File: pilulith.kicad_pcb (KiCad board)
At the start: 6 copper layers, 22.1 x 22.1 mm, 91 parts, among them J101 Conn_01x03_Pin, J103 Conn_ARM_JTAG_SWD_10, Q1 SBC847, SW1 KMT221NG, SW2 KMT221NG, U1 NRF54L15-QFAA-R, U10 LIS2DH, U102 WLA.04, U103 ATECC608B-MAHDA, U104 LF21115TMR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

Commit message: initial routing complete
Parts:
- removed C103: 10U, Capacitor_SMD:C_0805_2012Metric
- removed C106, C110, C112: 0.1U, Capacitor_SMD:C_0201_0603Metric
- removed C111: 4U7, Capacitor_SMD:C_0603_1608Metric
- removed C113, C114, C115, C116: 12P, Capacitor_SMD:C_0201_0603Metric
- removed TP1, TP16, TP17, TP18, TP19, TP2, TP20, TP3, TP4, TP5, TP6, TP7, TP8, TP9: TestPoint, TestPoint:TestPoint_Pad_D1.5mm
- added C3: 2U2, Capacitor_SMD:C_0201_0603Metric, F.Cu at (158.4, 93.7)
- added C4: 10N, Capacitor_SMD:C_0201_0603Metric, F.Cu at (159.9, 94.4)
- added C5: 2N2, Capacitor_SMD:C_0201_0603Metric, F.Cu at (165.6, 97.0)
- added C6: 0.1U, Capacitor_SMD:C_0201_0603Metric, F.Cu at (155.1, 99.9)
- added C7: 2U2, Capacitor_SMD:C_0201_0603Metric, F.Cu at (155.0, 94.5)
- added C8: 1P2, Capacitor_SMD:C_0201_0603Metric, F.Cu at (167.1, 99.2)
- added C9: 0.1U, Capacitor_SMD:C_0201_0603Metric, F.Cu at (160.8, 102.4)
- added L1: FB, Inductor_SMD:L_0201_0603Metric, F.Cu at (158.5, 94.4)
- added L3: 4U7, Inductor_SMD:L_0402_1005Metric, F.Cu at (156.8, 94.3)
- added L4: 2N0, Inductor_SMD:L_0201_0603Metric, F.Cu at (168.1, 99.6)
- added LED13: RED, LED_SMD:LED_0201_0603Metric, F.Cu at (159.3, 102.4)
- added LED14: RED, LED_SMD:LED_0201_0603Metric, F.Cu at (161.2, 104.0)
- added LED15: RED, LED_SMD:LED_0201_0603Metric, F.Cu at (159.5, 105.7)
- added LED16: RED, LED_SMD:LED_0201_0603Metric, F.Cu at (157.8, 104.0)
- added R1: R_Small, Resistor_SMD:R_0201_0603Metric, F.Cu at (157.9, 102.4)
- added R2: R_Small, Resistor_SMD:R_0201_0603Metric, F.Cu at (157.4, 105.9)
- added R3: R_Small, Resistor_SMD:R_0201_0603Metric, F.Cu at (157.0, 104.0)
- added R5: R_Small, Resistor_SMD:R_0201_0603Metric, F.Cu at (162.0, 104.0)
- added SW3: KMT221NG, Button_Switch_SMD:SW_Push_1P1T_NO_CK_KMR2, B.Cu at (151.9, 99.3)
- added SW4: KMT221NG, pilulith:SW_EVP-AWED4A, F.Cu at (164.0, 106.0)
- C108: value 1U -> 10U
- C117: value 12P -> 1P2
- G***: moved to F.Cu
- moved TP15 18.5 mm to (160.4, 113.6)
- moved U105 17.3 mm to (165.9, 110.7), turned to -45 degrees
- moved TP14 17.0 mm to (156.7, 113.4)
- moved U104 17.0 mm to (167.9, 106.3), turned to -22.5 degrees
- moved SW1 16.7 mm to (165.4, 97.5), turned to 135 degrees
- moved SW2 16.6 mm to (165.7, 110.4), turned to 45 degrees
- moved U106 16.3 mm to (151.2, 101.7), turned to -105 degrees
- moved C102 16.0 mm to (151.1, 106.3), turned to -165 degrees
- moved C108 11.4 mm to (154.2, 96.4), turned to 180 degrees
- moved C107 11.2 mm to (155.5, 95.6), turned to 90 degrees
- moved R114 10.3 mm to (152.8, 97.7), turned to 90 degrees
- moved C118 9.79 mm to (164.1, 109.9), turned to 45 degrees
- moved G*** 9.43 mm to (165.1, 102.1), turned to 120 degrees
- moved C101 8.99 mm to (163.4, 95.3), turned to 90 degrees
- moved R113 8.95 mm to (153.5, 97.7), turned to -90 degrees
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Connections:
- C107 pad 1: unconnected-(C107-Pad1) -> VCC
- C108 pad 1: /DEC4_6 -> VCC
- L102 pad 2: /ANT_FEED -> Net-(C8-Pad2)
- R113 pad 1: Net-(U1-P1.11/ASO(3)/RADIO(2)/AIN4) -> /BATTERY_MEAS
- R114 pad 2: Net-(U1-P1.11/ASO(3)/RADIO(2)/AIN4) -> /BATTERY_MEAS
- U1 pad 10: Net-(U1-VDD-Pad10) -> VCC
- U1 pad 11: /LED03 -> /LED11
- U1 pad 12: /LED08 -> /LED10
- U1 pad 13: /LED07 -> /LED09
- U1 pad 14: /LED06 -> /LED08
- U1 pad 15: /LED10 -> /LED07
- U1 pad 16: /LED11 -> /LED06
- U1 pad 17: /2.06/TC -> /LED05
- U1 pad 22: Net-(U1-VDD-Pad10) -> VCC
- U1 pad 28: /LED05 -> /LED03
- U1 pad 32: unconnected-(U1-VSS_PA-Pad32) -> GND
- U1 pad 33: unconnected-(U1-DECRF-Pad33) -> DECA
- U1 pad 36: Net-(U1-VDD-Pad10) -> VCC
- U1 pad 37: /LED01 -> /LED02
- U1 pad 38: /LED02 -> /LED01
- U1 pad 39: Net-(U1-P1.11/ASO(3)/RADIO(2)/AIN4) -> /IMU_INT
- U1 pad 43: unconnected-(U1-DECA-Pad43) -> DECA
- U1 pad 44: Net-(U1-VSS-Pad44) -> GND
- U1 pad 45: unconnected-(U1-DECD-Pad45) -> DECD
- U1 pad 46: unconnected-(U1-DCC-Pad46) -> DCC
- U1 pad 47: Net-(U1-VDD-Pad10) -> VCC
- U1 pad 48: Net-(U1-VDD-Pad10) -> VCC
- U1 pad 49: Net-(U1-VSS-Pad44) -> GND
- U1 pad 7: /IMU_INT -> /BATTERY_MEAS
- Y101 pad 2: GND -> unconnected-(Y101-Pad2)
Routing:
- net /BOOT: track 0.00 -> 52.6 mm, vias 0 -> 7
- net /SCL: track 0.00 -> 27.9 mm, vias 0 -> 5
- net /SDA: track 0.00 -> 23.6 mm, vias 0 -> 4
- net /MAG: track 0.00 -> 19.4 mm, vias 0 -> 3
- net /IMU_INT: track 0.00 -> 18.8 mm, vias 0 -> 3
- net VCC: track 0.00 -> 18.8 mm, vias 0 -> 21
- net /nRF52_RX: track 0.00 -> 18.4 mm, vias 0 -> 4
- net GND: track 0.00 -> 17.4 mm, vias 0 -> 52
- net /LED04: track 0.00 -> 17.3 mm, vias 0 -> 4
- net /LED05: track 0.00 -> 16.9 mm, vias 0 -> 3
- net /nRF52_TX: track 0.00 -> 16.6 mm, vias 0 -> 2
- net /SWCLK: track 0.00 -> 15.3 mm, vias 0 -> 2
- net /NFC1: track 0.00 -> 14.6 mm, vias 0 -> 3
- net /LED08: track 0.00 -> 14.3 mm, vias 0 -> 3
- net /LED06: track 0.00 -> 14.2 mm, vias 0 -> 2
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- removed copper zone on F.Cu, net VCC
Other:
- board text added: "HSM"
- board text added: "nRF54L"
- board text removed: "0.07"
- board text removed: "1.00"
- board text removed: "Boot/User"
- board text removed: "GND"
- board text removed: "SWCLK"
- board text removed: "SWDIO"
- board text removed: "VCC"

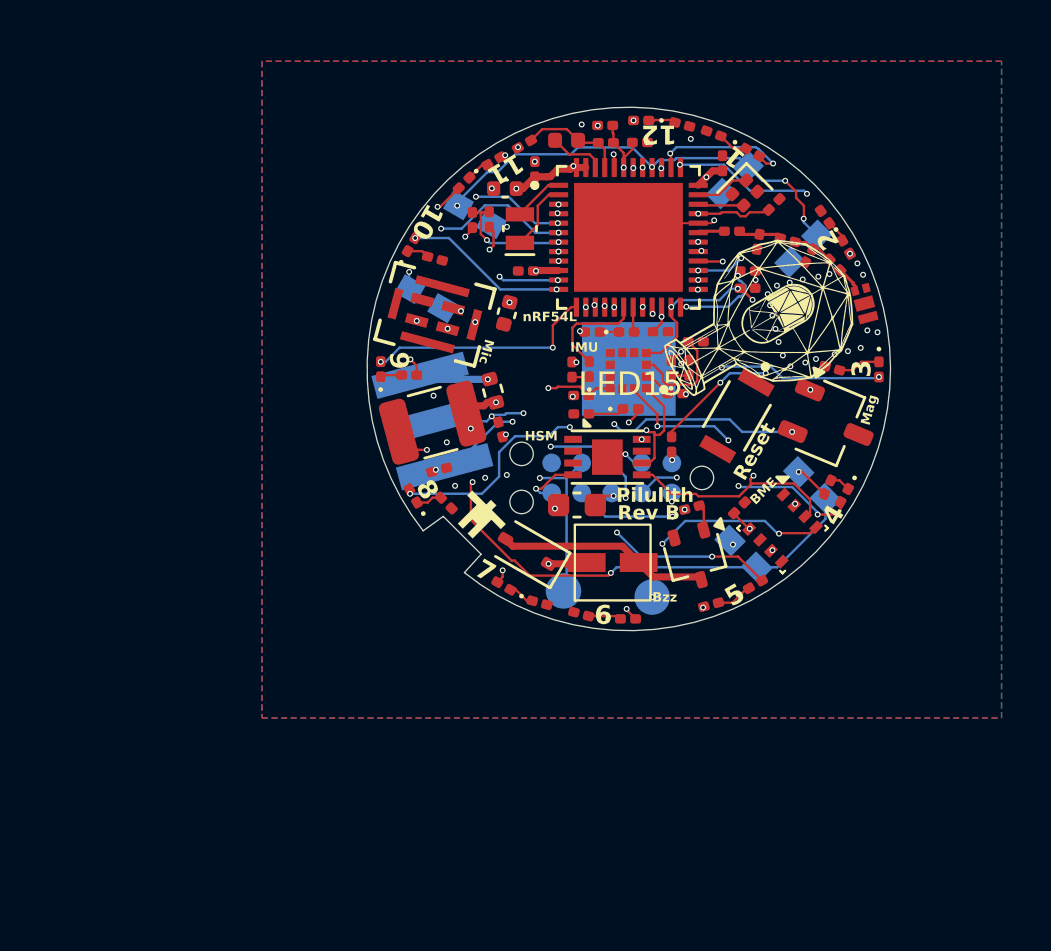
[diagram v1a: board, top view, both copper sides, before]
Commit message: putting in a no popped npm2100 for future proofing
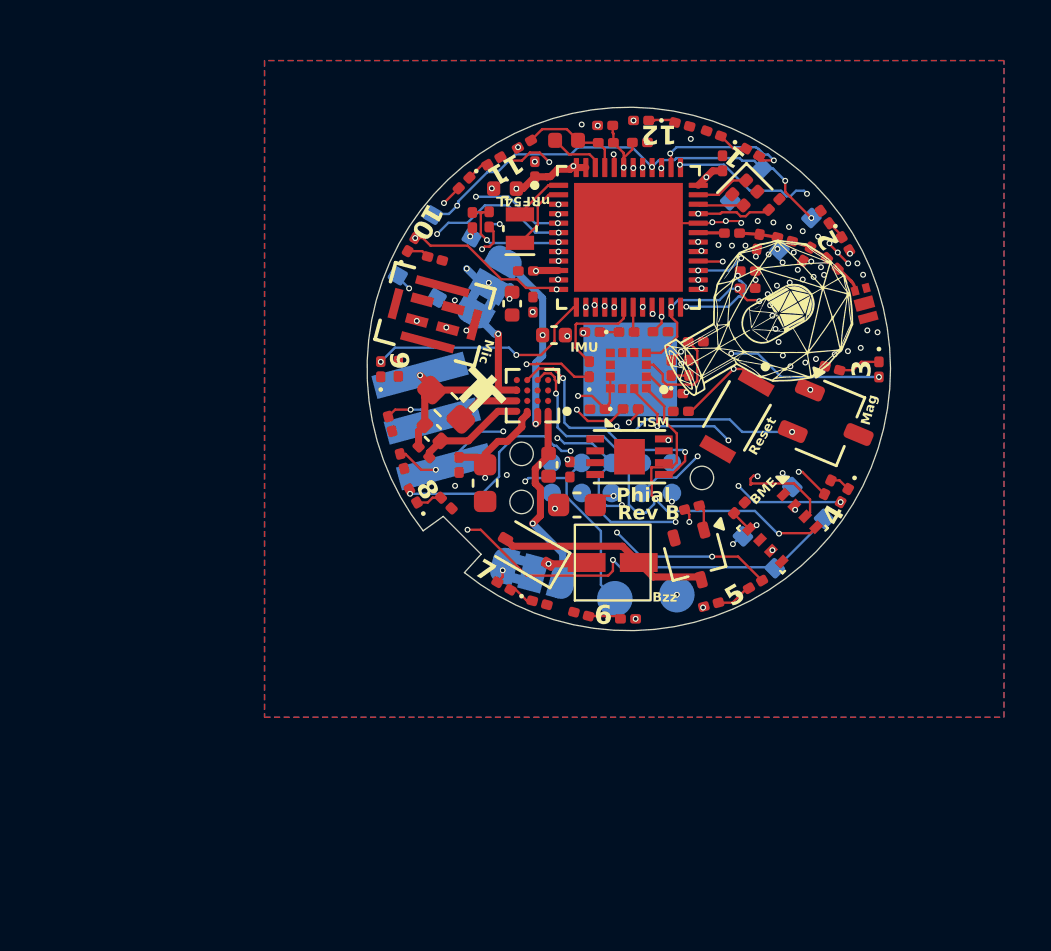
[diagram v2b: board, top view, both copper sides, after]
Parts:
- removed C102: 100U, Capacitor_SMD:C_1210_3225Metric
- removed R116: 0, Resistor_SMD:R_0402_1005Metric
- added C10: 22U, Capacitor_SMD:C_0603_1608Metric, F.Cu at (153.4, 108.8)
- added C11: 1N, Capacitor_SMD:C_0201_0603Metric, F.Cu at (150.8, 107.5)
- added C12: 10U, Capacitor_SMD:C_0402_1005Metric, F.Cu at (151.2, 106.7)
- added C13: 2U2, Capacitor_SMD:C_0402_1005Metric, F.Cu at (156.0, 108.0)
- added C14: 2U2, Capacitor_SMD:C_0402_1005Metric, F.Cu at (156.3, 102.6)
- added C16: 1N, Capacitor_SMD:C_0201_0603Metric, F.Cu at (152.3, 108.1)
- added G***: LOGO, orleon:the_golioth_2mm, B.Cu at (168.2, 109.0)
- added G***: LOGO, orleon:the_golioth_2mm, B.Cu at (151.1, 109.8)
- added JP1: npm2100-bridge, Jumper:SolderJumper-3_P1.3mm_Bridged2Bar12_RoundedPad1.0x1.5mm, B.Cu at (153.5, 100.5)
- added JP2: sensor-bridge, Jumper:SolderJumper-3_P1.3mm_Bridged2Bar12_RoundedPad1.0x1.5mm, B.Cu at (155.4, 112.6)
- added L2: 2u2, Inductor_SMD:L_0603_1608Metric_Pad1.05x0.95mm_HandSolder, F.Cu at (151.7, 105.5)
- added U2: NPM2100-CAAA-R, pilulith:BGA16N44P4X4_189X191X52N, F.Cu at (155.4, 105.1)
- SW1, SW2, SW3: footprint Button_Switch_SMD:SW_Push_1P1T_NO_CK_KMR2 -> pilulith:KMT221NG
- moved G*** 10.8 mm to (159.5, 93.8), turned to 0 degrees
- moved G*** 5.30 mm to (153.2, 104.9)
- moved C2 4.66 mm to (149.4, 106.3)
- moved R3 3.20 mm to (155.4, 101.3)
- moved R2 2.39 mm to (156.9, 108.2), turned to -90 degrees
- moved TP14 2.19 mm to (158.8, 113.7)
- moved C1 1.61 mm to (149.9, 107.9), turned to -75 degrees
- moved R66 1.45 mm to (161.6, 105.8), turned to 180 degrees
- moved TP15 1.04 mm to (161.5, 113.5)
- moved U103 0.94 mm to (159.5, 107.7)
- moved C105 0.90 mm to (158.1, 105.7)
- moved SW3 0.67 mm to (151.2, 99.2)
- moved R109 0.53 mm to (149.7, 104.0), turned to 90 degrees
- moved C104 0.47 mm to (154.5, 101.2), turned to -90 degrees
- moved SW2 0.42 mm to (166.0, 110.7)
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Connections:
- C104 pad 1: VCC -> VSENSOR
- C105 pad 1: VCC -> VSENSOR
- C118 pad 1: VCC -> VSENSOR
- C29 pad 1: VCC -> VSENSOR
- D3 pad 1: VCC -> VSENSOR
- LS1 pad 1: VCC -> VSENSOR
- R115 pad 2: VCC -> VSENSOR
- R117 pad 1: VCC -> VSENSOR
- R118 pad 1: VCC -> VSENSOR
- U10 pad 10: VCC -> VSENSOR
- U10 pad 9: VCC -> VSENSOR
- U103 pad 8: VCC -> VSENSOR
- U104 pad 1: VCC -> VSENSOR
- U105 pad 6: VCC -> VSENSOR
- U105 pad 8: VCC -> VSENSOR
- U106 pad 1: VCC -> VSENSOR
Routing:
- net /VOUT-NPM2100: track 0.00 -> 8.26 mm, vias 0 -> 2
- net /VOUTLDO-NPM2100: track 0.00 -> 8.18 mm, vias 0 -> 1
- net VSENSOR: track 0.00 -> 8.05 mm, vias 0 -> 11
- net /CR2032_V+: track 3.06 -> 10.9 mm, vias 1 -> 2
- net VCC: track 18.8 -> 11.7 mm, vias 21 -> 10
- net /SDA: track 23.6 -> 30.0 mm, vias 4 -> 6
- net /NFC1: track 14.6 -> 20.1 mm
- net /SCL: track 27.9 -> 33.0 mm
- net Net-(U2-PVSS): track 0.00 -> 4.62 mm
- net Net-(LED16-K): track 0.74 -> 5.24 mm, vias 0 -> 2
- net /VINT-NPM2100: track 0.00 -> 4.46 mm
- net Net-(LED15-K): track 1.53 -> 4.90 mm, vias 0 -> 2
- net GND: track 17.4 -> 14.3 mm, vias 52 -> 66
- net /nRF52_TX: track 16.6 -> 19.6 mm
- net /SW: track 0.00 -> 2.69 mm
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- added copper zone on In2.Cu, net VSENSOR
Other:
- board text added: "Phial"
- board text removed: "Pilulith"
- board text removed: "RST"

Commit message: rev b first pass done with no violatio ns
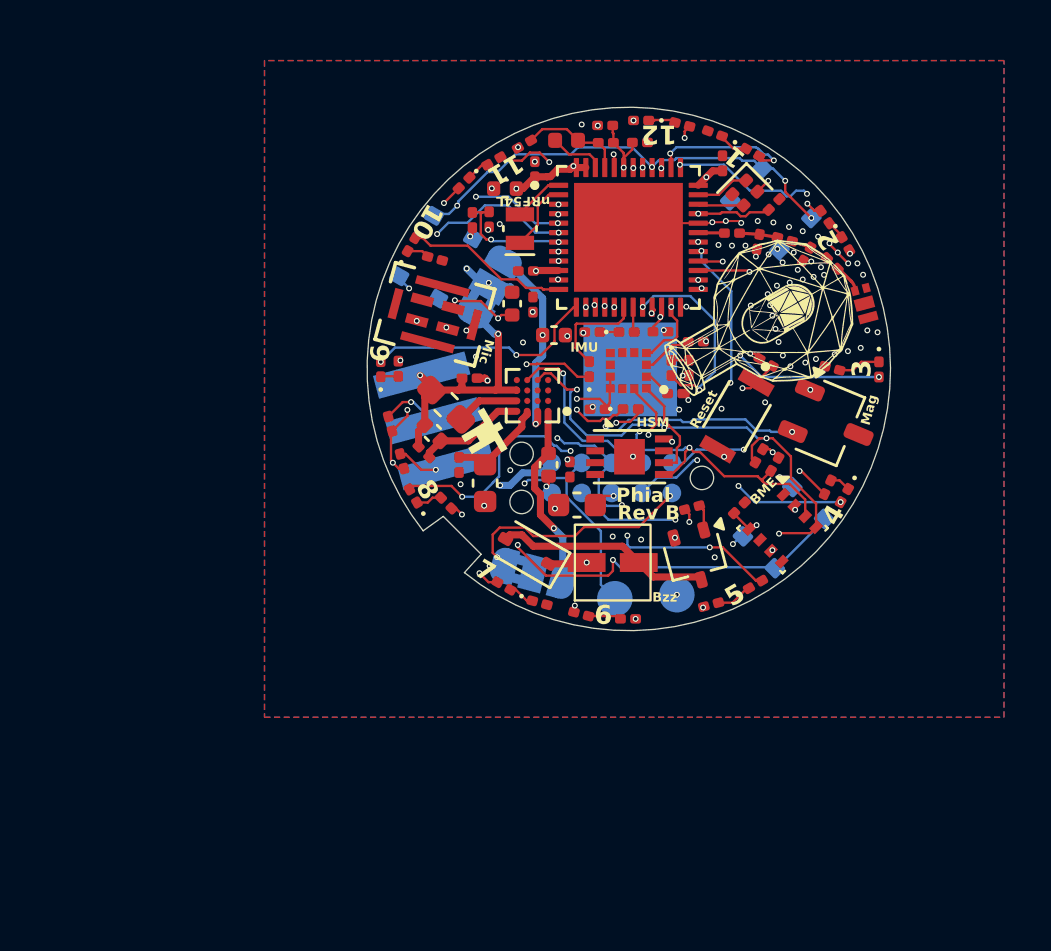
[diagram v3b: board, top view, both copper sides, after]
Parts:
- added R6: 0, Resistor_SMD:R_0201_0603Metric, F.Cu at (152.7, 104.4)
- moved R117 7.82 mm to (164.9, 107.7), turned to -120 degrees
- moved R118 7.53 mm to (165.6, 108.0), turned to -120 degrees
- moved R66 4.15 mm to (165.2, 103.7), turned to 150 degrees
- moved G*** 1.85 mm to (153.3, 106.8), turned to -60 degrees
- moved J101 0.07 mm to (151.2, 106.2)
- moved SW3 0.07 mm to (151.3, 99.3)
- turned C104 to 90 degrees
- turned LED14 to -90 degrees
- turned R5 to -90 degrees
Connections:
- J103 pad 6: unconnected-(J103-SWO/TDO-Pad6) -> /Power_Insert
- U105 pad 2: VCC -> VSENSOR
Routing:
- net GND: track 14.3 -> 24.7 mm, vias 66 -> 89
- net VCC: track 11.7 -> 20.7 mm, vias 10 -> 11
- net Net-(J103-~{RESET}): track 0.00 -> 7.92 mm, vias 0 -> 2
- net /Power_Insert: track 0.00 -> 7.70 mm, vias 0 -> 2
- net /2.09/T2: track 3.84 -> 8.35 mm
- net VSENSOR: track 8.05 -> 11.2 mm, vias 11 -> 12
- net /NFC1: track 20.1 -> 17.0 mm, vias 3 -> 2
- net Net-(U10-SDO/SA0): track 4.55 -> 2.17 mm
- net /SCL: track 33.0 -> 31.0 mm
- net /IMU_INT: track 17.8 -> 16.1 mm, vias 3 -> 2
- net /SDA: track 30.0 -> 28.7 mm, vias 6 -> 4
- net /LED07: track 13.6 -> 15.0 mm
- net /RESET_N: track 9.94 -> 8.74 mm
- net /2.10/T3: track 6.03 -> 6.97 mm
- net Net-(D109-K): track 0.10 -> 0.85 mm
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
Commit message: added second notch and moved associated components
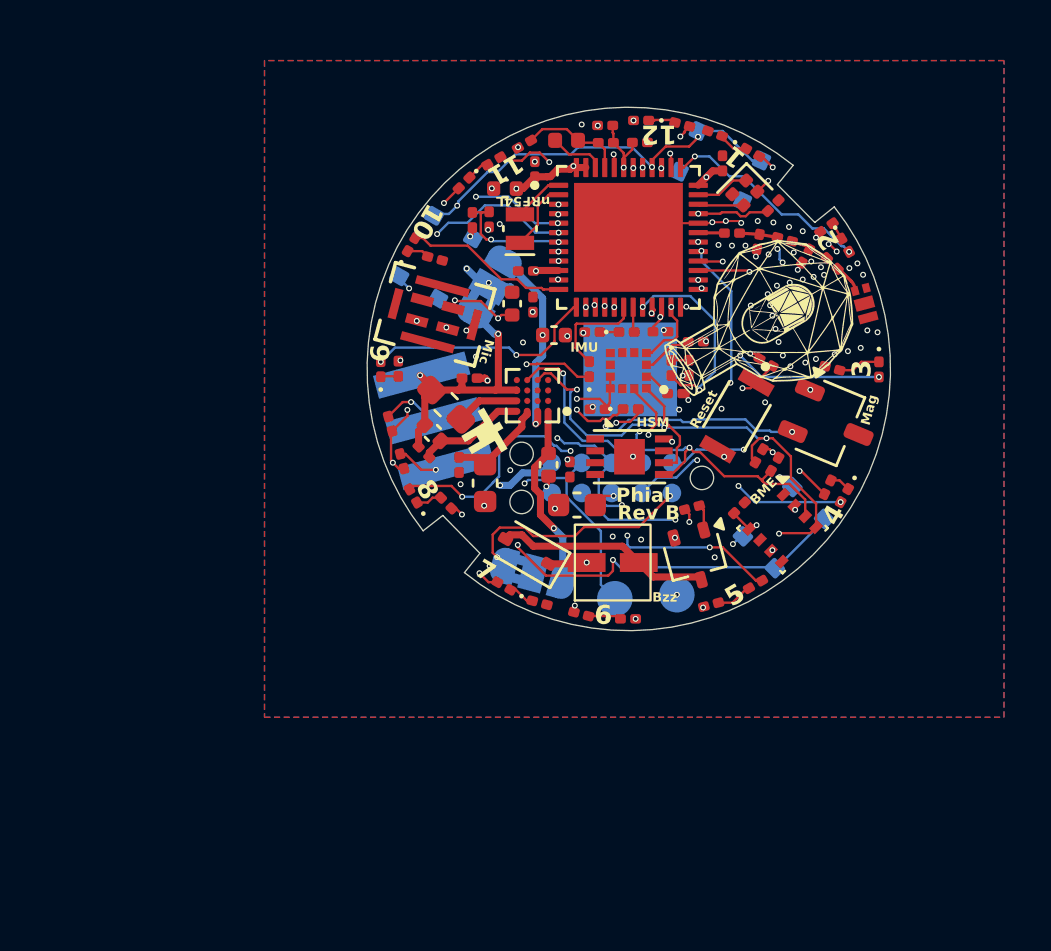
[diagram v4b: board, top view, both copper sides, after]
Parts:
- moved SW1 2.80 mm to (163.3, 95.4), turned to 155 degrees
- moved R102 0.45 mm to (167.8, 98.0), turned to -145 degrees
- moved C8 0.09 mm to (166.9, 99.2)
- moved C5 0.06 mm to (165.5, 97.1)
- moved D102 0.06 mm to (168.6, 98.8)
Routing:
- net /BOOT: track 53.9 -> 51.8 mm, vias 7 -> 6
- net GND: track 24.7 -> 23.4 mm, vias 89 -> 88
- net /LED02: track 9.50 -> 9.06 mm, vias 3 -> 2
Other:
- outline, holes or cut-outs redrawn

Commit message: add updated spirulo design into 3d space
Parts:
- moved G*** 1.47 mm to (167.6, 107.7)
- moved G*** 1.27 mm to (152.4, 109.7), turned to 135 degrees
- moved G*** 0.94 mm to (159.5, 94.8)
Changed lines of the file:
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@@
+			)
+		)
+		(model "${KIPRJMOD}/input/3d/spirulo-b-202601201651.step"
+			(offset
+				(xyz 0 0 4)
+			)
+			(scale
+				(xyz 1 1 1)
+			)
+			(rotate
+				(xyz -0 -0 -80)
 			)
 		)
@@
 	(footprint "orleon:the_golioth_2mm"
 		(layer "B.Cu")
-		(at 159.514483 93.807892)
+		(at 159.545315 94.75)
 		(property "Reference" "G***"
 			(at 0 0 0)
@@
 	(footprint "orleon:the_golioth_2mm"
 		(layer "B.Cu")
-		(at 168.22407 109.042462 -120)
+		(at 167.595315 107.71 -120)
 		(property "Reference" "G***"
 			(at 0 0 60)
@@
 	(footprint "orleon:the_golioth_2mm"
 		(layer "B.Cu")
-		(at 151.145315 109.8 120)
+		(at 152.405315 109.67 135)
 		(property "Reference" "G***"
-			(at 0 0 120)
+			(at 0 0 135)
 			(layer "B.SilkS")
 			(hide yes)
@@
 		)
 		(property "Value" "LOGO"
-			(at 0.75 0 120)
+			(at 0.75 0 135)
 			(layer "B.SilkS")
 			(hide yes)
@@
 		)
 		(property "Datasheet" ""
-			(at 0 0 120)
+			(at 0 0 135)
 			(layer "B.Fab")
 			(hide yes)
@@
 		)
 		(property "Description" ""
-			(at 0 0 120)
+			(at 0 0 135)
 			(layer "B.Fab")
 			(hide yes)
@@
 		(fp_poly
 			(pts
-				(xy 0.165428 0.712626) (xy 0.16543 0.572646) (xy 0.585368 0.572648) (xy 1.00531 0.572646) (xy 1.00531 0.419942)
-				(xy 1.005307 0.267237) (xy 0.725353 0.267234) (xy 0.445391 0.267235) (xy 0.44539 -0.292688) (xy 0.445391 -0.852604)
-				(xy 0.292684 -0.852605) (xy 0.139979 -0.852605) (xy 0.13998 -0.572645) (xy 0.139979 -0.292685) (xy -0.000001 -0.292685)
-				(xy -0.139981 -0.292685) (xy -0.139981 -0.572646) (xy -0.139981 -0.852606) (xy -0.29269 -0.852603)
+				(xy 0.165428 0.712626) (xy 0.16543 0.572646) (xy 0.585368 0.572648) (xy 1.00531 0.572645) (xy 1.00531 0.419942)
+				(xy 1.005307 0.267238) (xy 0.725353 0.267234) (xy 0.44539 0.267235) (xy 0.44539 -0.292688) (xy 0.445391 -0.852604)
+				(xy 0.292684 -0.852605) (xy 0.139979 -0.852605) (xy 0.13998 -0.572645) (xy 0.13998 -0.292685) (xy -0.000001 -0.292685)
+				(xy -0.139981 -0.292685) (xy -0.139981 -0.572645) (xy -0.139981 -0.852606) (xy -0.292689 -0.852603)
 				(xy -0.445387 -0.852605) (xy -0.445393 -0.292686) (xy -0.445392 0.267235) (xy -0.725352 0.267235)
-				(xy -1.005312 0.267235) (xy -1.005303 0.419938) (xy -1.00531 0.572645) (xy -0.585372 0.572646) (xy -0.165431 0.572648)
-				(xy -0.165431 0.712626) (xy -0.165432 0.852608) (xy -0.000002 0.852604) (xy 0.165429 0.852605)
-			)
-			(stroke
+				(xy -1.005311 0.267235) (xy -1.005303 0.419937) (xy -1.005309 0.572645) (xy -0.585372 0.572645)
+				(xy -0.16543 0.572648) (xy -0.16543 0.712626) (xy -0.165432 0.852608) (xy -0.000003 0.852604) (xy 0.165429 0.852605)
+			)
+			(stroke

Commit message: fix missing connections on npm2100
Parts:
- added R8: 0, Resistor_SMD:R_0201_0603Metric, F.Cu at (153.2, 99.5)
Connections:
- JP2 pad 2: unconnected-(JP2-C-Pad2) -> VSENSOR
- U2 pad C1: unconnected-(U2-PG/RESET-PadC1) -> /RESET_N
- U2 pad D4: unconnected-(U2-SHPHLD-PadD4) -> Net-(U2-SHPHLD)
- Y101 pad 2: unconnected-(Y101-Pad2) -> GND
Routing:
- net /RESET_N: track 8.74 -> 21.7 mm, vias 2 -> 4
- net Net-(U2-SHPHLD): track 0.00 -> 6.17 mm
- net /BOOT: track 51.8 -> 55.5 mm, vias 6 -> 7
- net VSENSOR: track 11.2 -> 12.8 mm, vias 12 -> 14
- net GND: track 23.4 -> 24.6 mm, vias 88 -> 94
